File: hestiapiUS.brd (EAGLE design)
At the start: 90 x 63 mm, 24 parts, among them U1 RPI-ZERO, U2 ULN2003AD, U3 LM2675MX-5.0/NOPBM08A-L, X1 MKDSN1,5/2-5,08, X2 MKDSN1,5/6-5,08

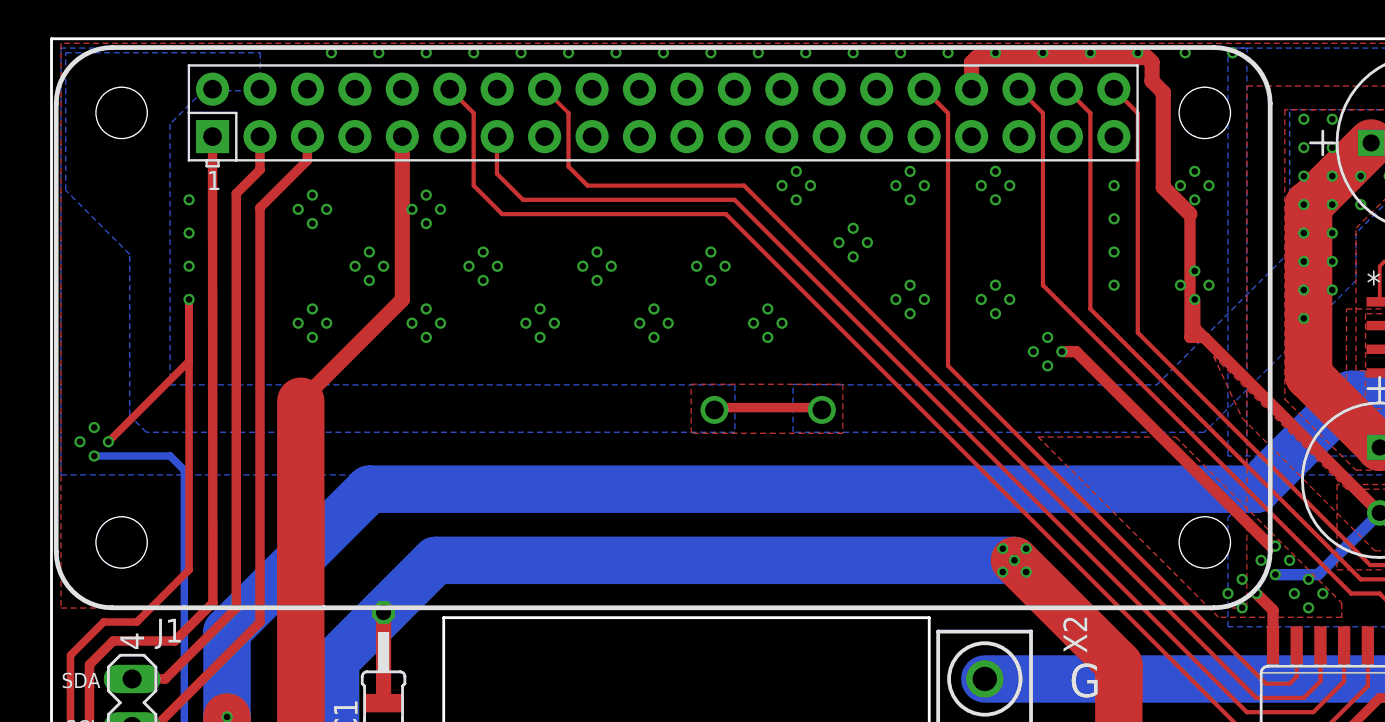
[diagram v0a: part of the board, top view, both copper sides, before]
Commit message: fix library pathing and add library
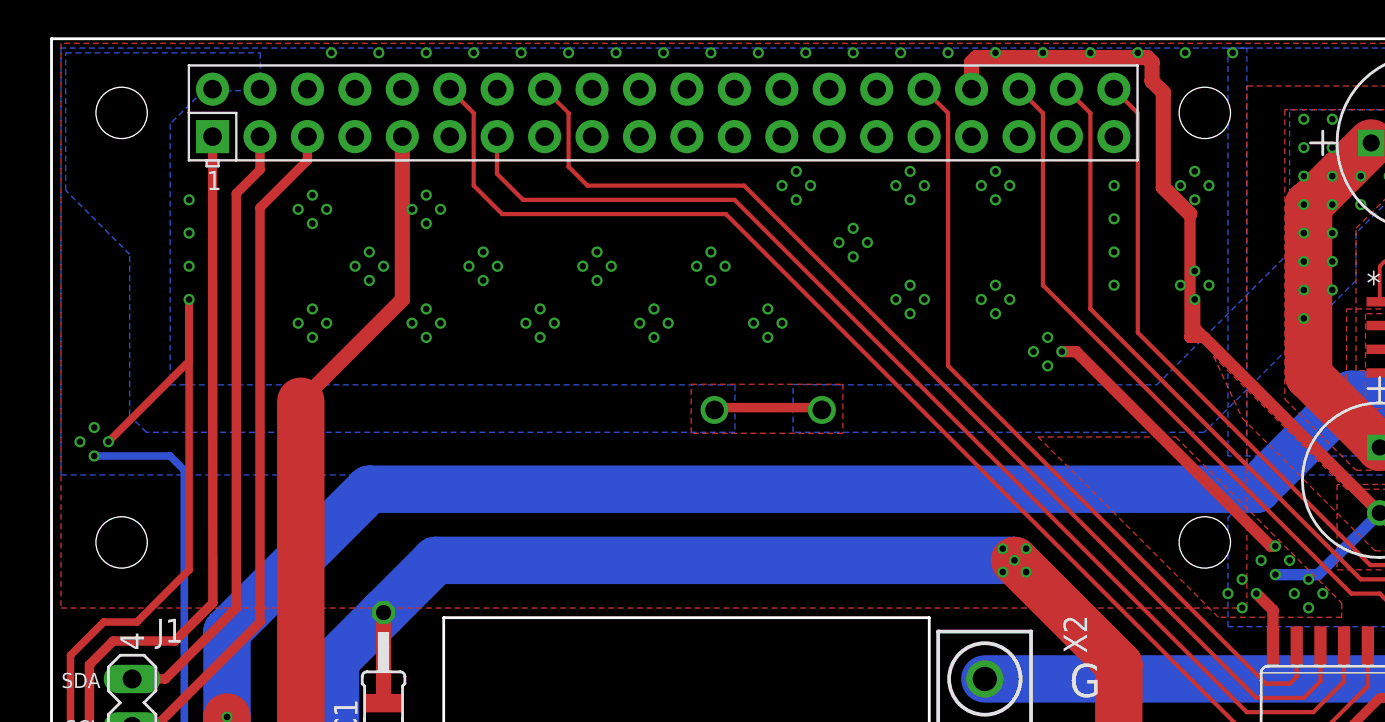
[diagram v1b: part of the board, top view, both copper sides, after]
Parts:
- BR1: device rectifier:DFS -> hestiapiUS:DFS
- C1: device obbgood:PCAP_12_5X20-THRU-ELECT -> hestiapiUS:PCAP_12_5X20-THRU-ELECT
- C2: value 0.1uF -> 0.01uF; device SparkFun-Capacitors:0603 -> hestiapiUS:0603
- C3: device obbgood:RR-A -> hestiapiUS:RR-A
- D1: device obbgood:DIODE_SMC_7P15X6P25 -> hestiapiUS:DIODE_SMC_7P15X6P25
- J1: device con-lstb:MA04-1 -> hestiapiUS:MA04-1
- JP1: device jumper:JP1 -> hestiapiUS:JP1
- KE, KG, KO, KW, KY, KY2: device obbgood:G6DN -> hestiapiUS:G6DN
- L1: device obbgood:IND_BOURNS_RLB0914 -> hestiapiUS:IND_BOURNS_RLB0914
- L2: device obbgood:IND_50XXXC -> hestiapiUS:IND_50XXXC
- PTC1: device obbgood:0ZCJ -> hestiapiUS:0ZCJ
- U1: device RPI-Zero:RASPBERRYPI_BASTELSTUBE_V13_RASPI_BOARD_B+_FULL -> hestiapiUS:RASPBERRYPI_BASTELSTUBE_V13_RASPI_BOARD_B+_FULL
- U2: device uln-udn:SO16 -> hestiapiUS:SO16
- U3: device obbgood:M08A-L -> hestiapiUS:M08A-L
- VR1: device obbgood:VARISTOR7MM -> hestiapiUS:VARISTOR7MM
- X1: device obbgood:MKDSN1,5/2-5,08 -> hestiapiUS:MKDSN1,5/2-5,08
- X2: device obbgood:MKDSN1,5/6-5,08 -> hestiapiUS:MKDSN1,5/6-5,08
